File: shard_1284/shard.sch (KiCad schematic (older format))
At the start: 7 parts, among them J0 Shard, J1 ISP, U1 ATmega1284P-MU, Y1 16MHz

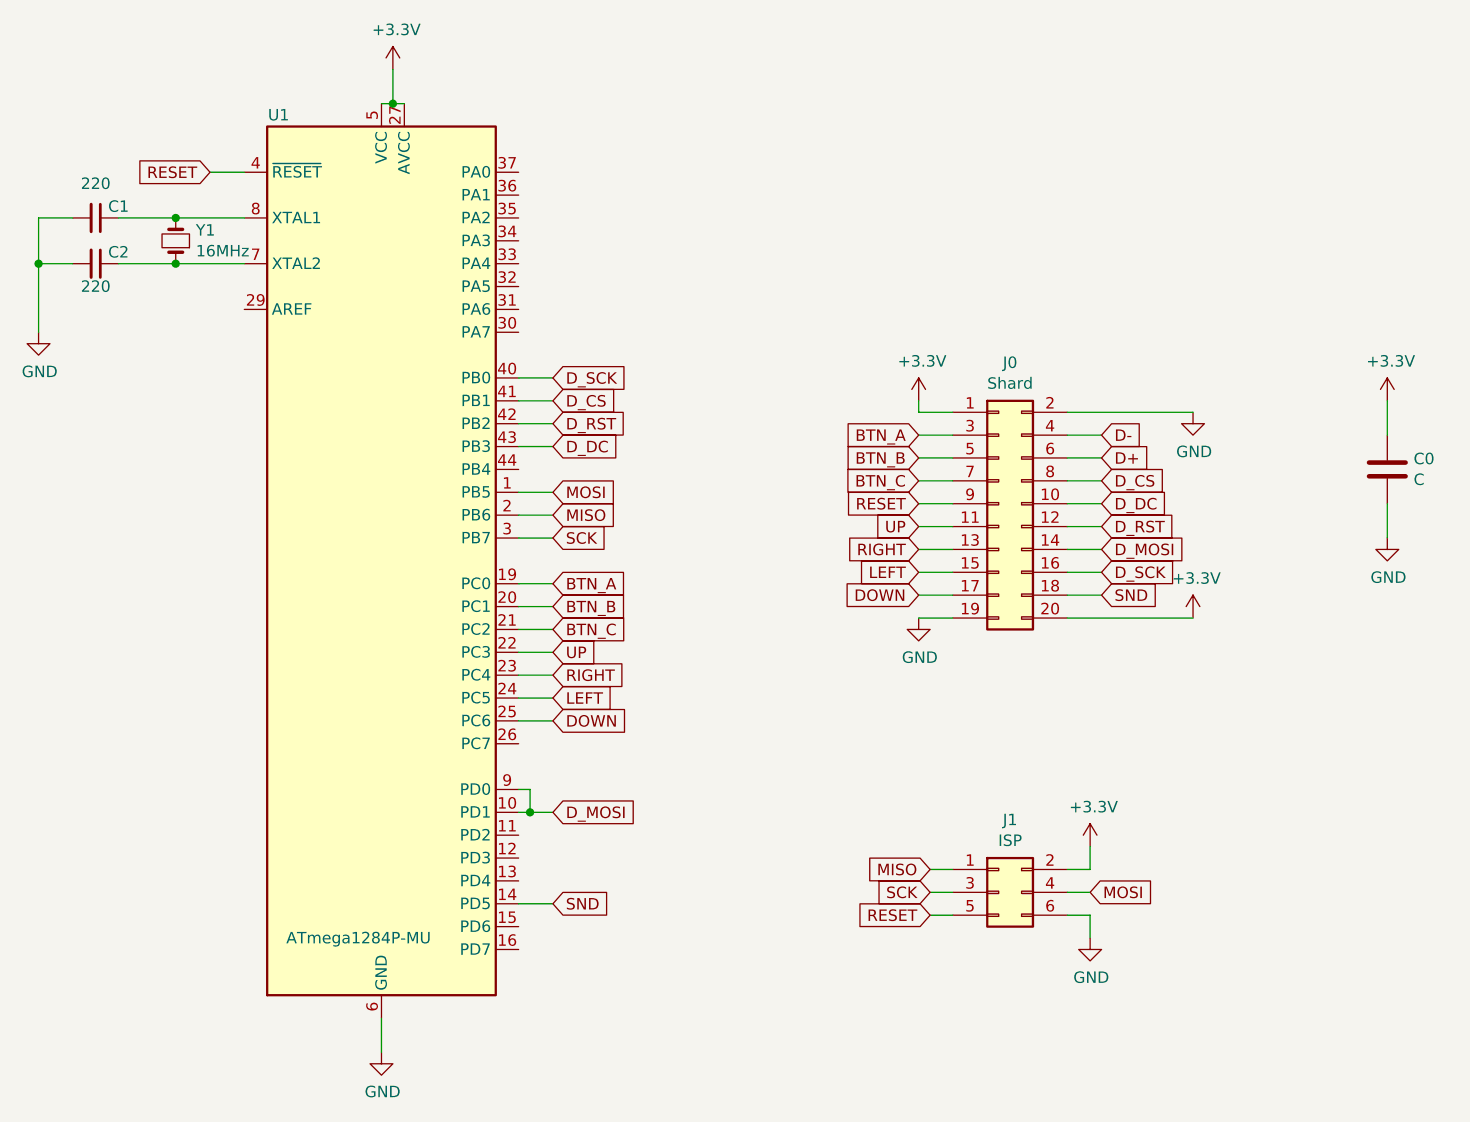
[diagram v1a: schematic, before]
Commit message: 1284 shard updated to edge connector
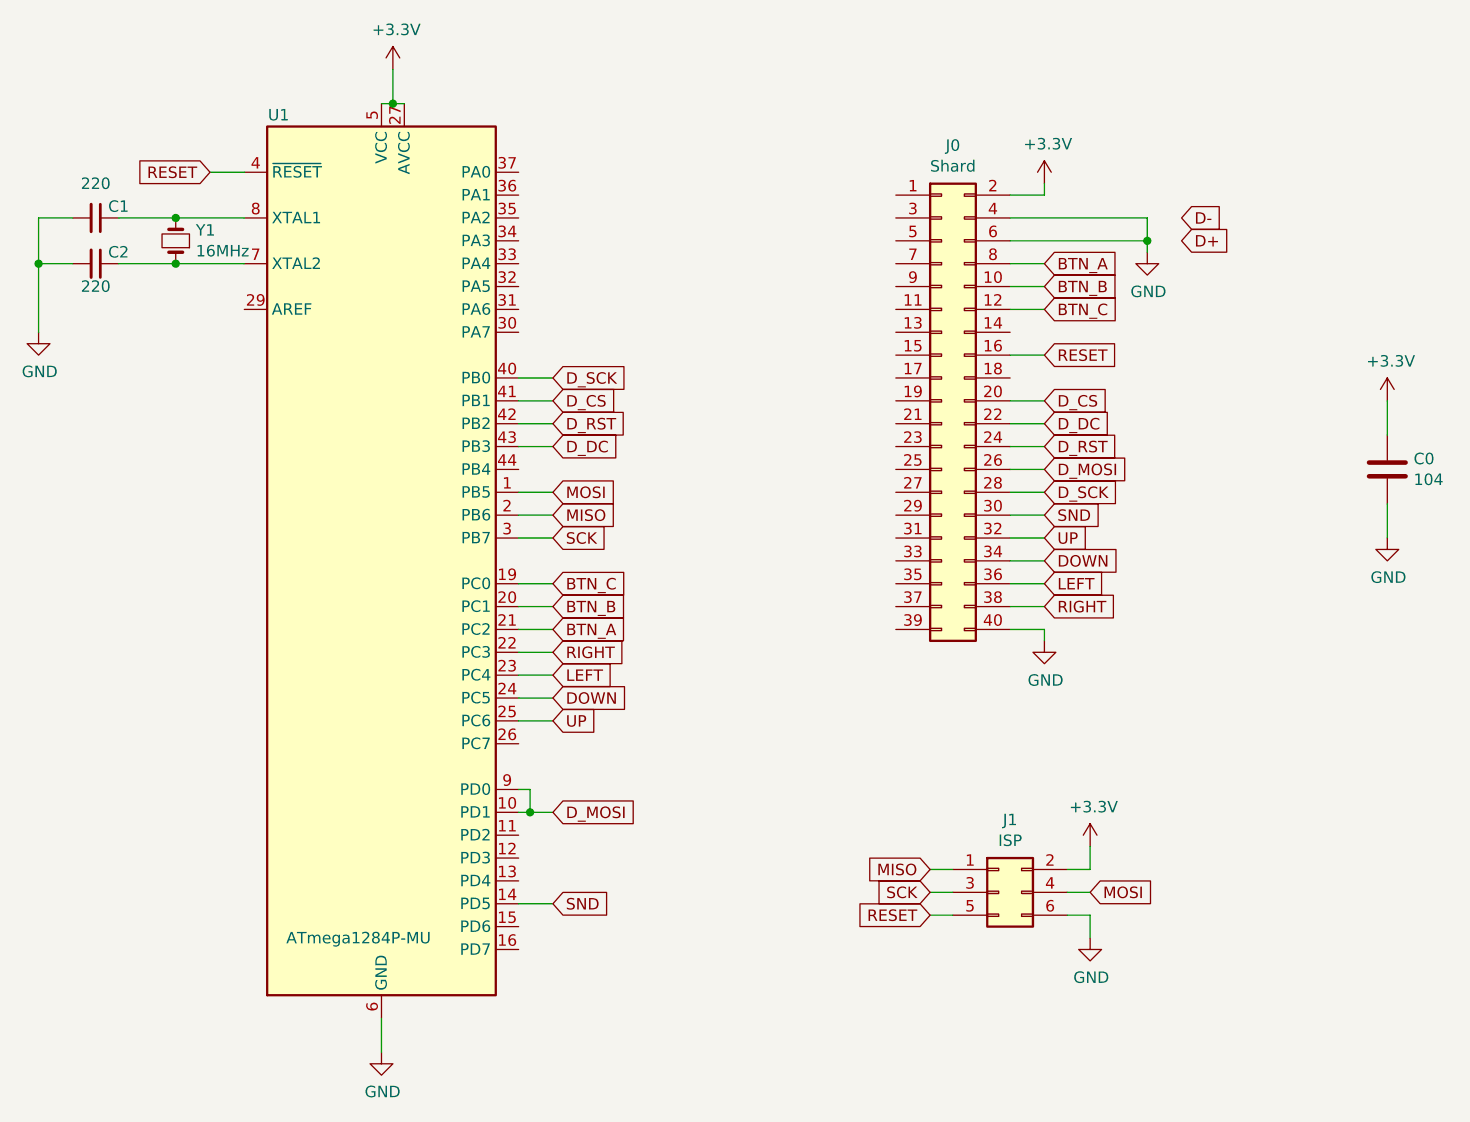
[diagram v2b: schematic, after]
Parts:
- removed J0: Shard, Connector_PinHeader_2.54mm:PinHeader_2x10_P2.54mm_Vertical, symbol Connector_Generic:Conn_02x10_Odd_Even
- added J0: Shard, Custom Footprints:Samtec_MEC8-120-02-L-D-RA1_Edge, symbol Connector_Generic:Conn_02x20_Odd_Even
- C0: value C -> 104
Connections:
- net +3V3: now also J0.2 (Pin_2)
- net BTN_A: now also U1.21 (PC2), J0.8 (Pin_8); no longer U1.19 (PC0)
- net BTN_B: now also J0.10 (Pin_10)
- net BTN_C: now also U1.19 (PC0), J0.12 (Pin_12); no longer U1.21 (PC2)
- net DOWN: now also U1.24 (PC5), J0.34 (Pin_34); no longer U1.25 (PC6)
- net D_CS: now also J0.20 (Pin_20)
- net D_DC: now also J0.22 (Pin_22)
- net D_MOSI: now also J0.26 (Pin_26)
- net D_RST: now also J0.24 (Pin_24)
- net D_SCK: now also J0.28 (Pin_28)
- net GND: now also J0.4 (Pin_4), J0.40 (Pin_40), J0.6 (Pin_6)
- net LEFT: now also U1.23 (PC4), J0.36 (Pin_36); no longer U1.24 (PC5)
- net RESET: now also J0.16 (Pin_16)
- net RIGHT: now also U1.22 (PC3), J0.38 (Pin_38); no longer U1.23 (PC4)
- net SND: now also J0.30 (Pin_30)
- net UP: now also U1.25 (PC6), J0.32 (Pin_32); no longer U1.22 (PC3)
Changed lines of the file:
@@
 $EndDescr
-$Comp
-L Connector_Generic:Conn_02x10_Odd_Even J0
-U 1 1 5BE693B2
-P 6100 3200
-F 0 "J0" H 6150 3817 50  0000 C CNN
-F 1 "Shard" H 6150 3726 50  0000 C CNN
-F 2 "Connector_PinHeader_2.54mm:PinHeader_2x10_P2.54mm_Vertical" H 6100 3200 50  0001 C CNN
-F 3 "~" H 6100 3200 50  0001 C CNN
-	1    6100 3200
-	1    0    0    -1
-$EndComp
 $Comp
 L Device:C C0
@@
 P 7800 3050
 F 0 "C0" H 7915 3096 50  0000 L CNN
-F 1 "C" H 7915 3005 50  0000 L CNN
+F 1 "104" H 7915 3005 50  0000 L CNN
 F 2 "Capacitor_THT:C_Rect_L7.0mm_W2.5mm_P5.00mm" H 7838 2900 50  0001 C CNN
 F 3 "~" H 7800 3050 50  0001 C CNN
@@
 L power:+3.3V #PWR0101
 U 1 1 5BE699E5
-P 5750 2750
-F 0 "#PWR0101" H 5750 2600 50  0001 C CNN
-F 1 "+3.3V" H 5765 2923 50  0000 C CNN
-F 2 "" H 5750 2750 50  0001 C CNN
-F 3 "" H 5750 2750 50  0001 C CNN
-	1    5750 2750
+P 6300 1800
+F 0 "#PWR0101" H 6300 1650 50  0001 C CNN
+F 1 "+3.3V" H 6315 1973 50  0000 C CNN
+F 2 "" H 6300 1800 50  0001 C CNN
+F 3 "" H 6300 1800 50  0001 C CNN
+	1    6300 1800
 	1    0    0    -1
 $EndComp
@@
 L power:GND #PWR0102
 U 1 1 5BE69B29
-P 5750 3700
-F 0 "#PWR0102" H 5750 3450 50  0001 C CNN
-F 1 "GND" H 5755 3527 50  0000 C CNN
-F 2 "" H 5750 3700 50  0001 C CNN
-F 3 "" H 5750 3700 50  0001 C CNN
-	1    5750 3700
+P 6300 3800
+F 0 "#PWR0102" H 6300 3550 50  0001 C CNN
+F 1 "GND" H 6305 3627 50  0000 C CNN
+F 2 "" H 6300 3800 50  0001 C CNN
+F 3 "" H 6300 3800 50  0001 C CNN
+	1    6300 3800
 	1    0    0    -1
 $EndComp
@@
 	1    0    0    -1
 $EndComp
-Wire Wire Line
-	5750 2750 5750 2800
-Wire Wire Line
-	5750 2800 5900 2800
-Text GLabel 6550 3100 2    50   Input ~ 0
+Text GLabel 6300 2750 2    50   Input ~ 0
 D_CS
-Text GLabel 6550 3200 2    50   Input ~ 0
+Text GLabel 6300 2850 2    50   Input ~ 0
 D_DC
-Text GLabel 6550 3300 2    50   Input ~ 0
+Text GLabel 6300 2950 2    50   Input ~ 0
 D_RST
-Text GLabel 6550 3400 2    50   Input ~ 0
+Text GLabel 6300 3050 2    50   Input ~ 0
 D_MOSI
-Text GLabel 6550 3500 2    50   Input ~ 0
+Text GLabel 6300 3150 2    50   Input ~ 0
 D_SCK
-Wire Wire Line
-	6400 2900 6550 2900
-Wire Wire Line
-	6400 3000 6550 3000
-Wire Wire Line
-	6400 3100 6550 3100
-Wire Wire Line
-	6400 3200 6550 3200
-Text GLabel 5750 3300 0    50   Input ~ 0
+Text GLabel 6300 3350 2    50   Input ~ 0
 UP
-Text GLabel 5750 3600 0    50   Input ~ 0
+Text GLabel 6300 3450 2    50   Input ~ 0
 DOWN
-Text GLabel 5750 3500 0    50   Input ~ 0
+Text GLabel 6300 3550 2    50   Input ~ 0
 LEFT
-Text GLabel 5750 3400 0    50   Input ~ 0
+Text GLabel 6300 3650 2    50   Input ~ 0
 RIGHT
-Text GLabel 6550 3600 2    50   Input ~ 0
+Text GLabel 6300 3250 2    50   Input ~ 0
 SND
-Text GLabel 5750 3200 0    50   Input ~ 0
+Text GLabel 6300 2550 2    50   Input ~ 0
 RESET
-Text GLabel 5750 3100 0    50   Input ~ 0
+Text GLabel 6300 2350 2    50   Input ~ 0
 BTN_C
-Text GLabel 5750 3000 0    50   Input ~ 0
+Text GLabel 6300 2250 2    50   Input ~ 0
 BTN_B
-Text GLabel 5750 2900 0    50   Input ~ 0
+Text GLabel 6300 2150 2    50   Input ~ 0
 BTN_A
-Wire Wire Line
-	5750 2900 5900 2900
-Wire Wire Line
-	5750 3000 5900 3000
-Wire Wire Line
-	5750 3100 5900 3100
-Wire Wire Line
-	5750 3200 5900 3200
-Wire Wire Line
-	5750 3300 5900 3300
-Wire Wire Line
-	5750 3400 5900 3400
-Wire Wire Line
-	5750 3500 5900 3500
-Wire Wire Line
-	5750 3600 5900 3600
-Wire Wire Line
-	5750 3700 5900 3700
 $Comp
 L power:+3.3V #PWR0104
@@
 Wire Wire Line
 	7800 3200 7800 3350
-Text GLabel 6550 3000 2    50   Input ~ 0
+Text GLabel 6900 2050 2    50   Input ~ 0
 D+
-Text GLabel 6550 2900 2    50   Input ~ 0
+Text GLabel 6900 1950 2    50   Input ~ 0
 D-
 $Comp
@@
 	1    0    0    -1
 $EndComp
+Text GLabel 4150 4150 2    50   Input ~ 0
+UP
+Text GLabel 4150 4050 2    50   Input ~ 0
+DOWN
+Text GLabel 4150 3950 2    50   Input ~ 0
+LEFT
 Text GLabel 4150 3850 2    50   Input ~ 0
-UP
-Text GLabel 4150 4150 2    50   Input ~ 0
-DOWN
-Text GLabel 4150 4050 2    50   Input ~ 0
-LEFT
-Text GLabel 4150 3950 2    50   Input ~ 0
 RIGHT
-Text GLabel 4150 3750 2    50   Input ~ 0
+Text GLabel 4150 3550 2    50   Input ~ 0
 BTN_C
 Text GLabel 4150 3650 2    50   Input ~ 0
 BTN_B
-Text GLabel 4150 3550 2    50   Input ~ 0
+Text GLabel 4150 3750 2    50   Input ~ 0
 BTN_A
 Text GLabel 4150 2750 2    50   Input ~ 0
@@
 SND
 $Comp
-L power:GND #PWR02
-U 1 1 5BEC77E8
-P 6950 2800
-F 0 "#PWR02" H 6950 2550 50  0001 C CNN
-F 1 "GND" H 6955 2627 50  0000 C CNN
-F 2 "" H 6950 2800 50  0001 C CNN
-F 3 "" H 6950 2800 50  0001 C CNN
-	1    6950 2800
-	1    0    0    -1
-$EndComp
-$Comp
-L power:+3.3V #PWR03
-U 1 1 5BEC7B87
-P 6950 3700
-F 0 "#PWR03" H 6950 3550 50  0001 C CNN
-F 1 "+3.3V" H 6965 3873 50  0000 C CNN
-F 2 "" H 6950 3700 50  0001 C CNN
-F 3 "" H 6950 3700 50  0001 C CNN
-	1    6950 3700
-	1    0    0    -1
-$EndComp
-Wire Wire Line
-	6400 3700 6950 3700
-Wire Wire Line
-	6400 2800 6950 2800
-Wire Wire Line
-	6400 3300 6550 3300
-Wire Wire Line
-	6400 3400 6550 3400
-Wire Wire Line
-	6550 3500 6400 3500
-Wire Wire Line
-	6400 3600 6550 3600
-$Comp
 L Device:Crystal_Small Y1
 U 1 1 5BECE84F
@@
 Wire Wire Line
 	4050 4450 4050 4550
+$Comp
+L Connector_Generic:Conn_02x20_Odd_Even J0
+U 1 1 5BEAC9FA
+P 5850 2750
+F 0 "J0" H 5900 3867 50  0000 C CNN
+F 1 "Shard" H 5900 3776 50  0000 C CNN
+F 2 "Custom Footprints:Samtec_MEC8-120-02-L-D-RA1_Edge" H 5850 2750 50  0001 C CNN
+F 3 "~" H 5850 2750 50  0001 C CNN
+	1    5850 2750
+	1    0    0    -1
+$EndComp
+Wire Wire Line
+	6150 1850 6300 1850
+Wire Wire Line
+	6300 1850 6300 1800
+Wire Wire Line
+	6300 2150 6150 2150
+Wire Wire Line
+	6150 2250 6300 2250
+Wire Wire Line
+	6300 2350 6150 2350
+Wire Wire Line
+	6150 2550 6300 2550
+Wire Wire Line
+	6300 2750 6150 2750
+Wire Wire Line
+	6150 2850 6300 2850
+Wire Wire Line
+	6300 2950 6150 2950
+Wire Wire Line
+	6150 3050 6300 3050
+Wire Wire Line
+	6300 3150 6150 3150
+Wire Wire Line
+	6150 3250 6300 3250
+Wire Wire Line
+	6300 3350 6150 3350
+Wire Wire Line
+	6150 3450 6300 3450
+Wire Wire Line
+	6300 3550 6150 3550
+Wire Wire Line
+	6150 3650 6300 3650
+Wire Wire Line
+	6150 3750 6300 3750
+Wire Wire Line
+	6300 3750 6300 3800
+$Comp
+L power:GND #PWR?
+U 1 1 5BEC5C1D
+P 6750 2100
+F 0 "#PWR?" H 6750 1850 50  0001 C CNN
+F 1 "GND" H 6755 1927 50  0000 C CNN
+F 2 "" H 6750 2100 50  0001 C CNN
+F 3 "" H 6750 2100 50  0001 C CNN
+	1    6750 2100
+	1    0    0    -1
+$EndComp
+Wire Wire Line
+	6750 2050 6750 2100
+Wire Wire Line
+	6150 2050 6750 2050
+Wire Wire Line
+	6750 1950 6750 2050
+Wire Wire Line
+	6150 1950 6750 1950
+Connection ~ 6750 2050
 $EndSCHEMATC
